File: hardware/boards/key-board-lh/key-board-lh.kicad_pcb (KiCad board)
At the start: 2 copper layers, 84 x 42 mm, 35 parts

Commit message: LH key board: every key's network identical round its switch; no acid traps; silk both sides
Owner: "the components for keys should be exactly spaced the exact same
way around every single key".
- layout.yaml networks: is ONE pattern relative to each key's switch (from
  the body CAD): the T's junction 10 mm along the body, S and P across it,
  C toward the key. On this board the one offset that clears every
  switch's pins and pole, J-CHAIN, the test pads, the register, the
  standoffs and the edge for all five keys; except: holds any key that
  cannot take it, with its reason (none here).
- Their silk letters and key name are one fixed arrangement round each T;
  a label that does not fit stops the layout rather than wandering.
- Test pads in the register's pin order (SER, QH ... 3V3), and route_first
  for the nets that reach J-CHAIN's far row, which only its back can reach.

Traces: 0 acute junctions (were 4), and a new pcb.py check fails on any -
verified to report all four on the previous board. Stitching vias keep 90
degrees from every track already on a pad (a routed pad goes without one
rather than make a wedge); a route joining the tree at a bend is squared
to a right-angle T where its clearance allows.

Silkscreen: the switch side now carries each key's name, J-CHAIN's pin-1
dot and mouth arrow (it is soldered from that side), MOUTH and the title;
the parts side adds CB DNP and MOUTH. Labels keep 0.25 mm apart and off
every pad and hole, the title lines 1.8 lines apart (0.117 mm failed).

Co-Authored-By: Claude Opus 5.5 <noreply@anthropic.com>
Claude-Session: https://claude.ai/code/session_01LmB4muFXnoLprWX4JzuJ5A
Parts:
- moved R-KEY-SER-LH5 18.6 mm to (178.0, 115.2), turned to 90 degrees
- moved R-KEY-SER-LH4 17.9 mm to (178.0, 133.2), turned to 90 degrees
- moved TP-3V3-LH 15.5 mm to (160.5, 114.0)
- moved R-KEY-PU-LH2 15.5 mm to (140.0, 118.8), turned to 90 degrees
- moved R-KEY-PU-LH3 15.5 mm to (160.0, 118.8), turned to 90 degrees
- moved C-KEY-LH2 15.5 mm to (137.3, 121.5), turned to 180 degrees
- moved C-KEY-LH3 15.5 mm to (157.3, 121.5), turned to 180 degrees
- moved R-KEY-SER-LH1 15.4 mm to (120.0, 124.2), turned to 90 degrees
- moved R-KEY-SER-LH2 15.2 mm to (140.0, 124.2), turned to 90 degrees
- moved R-KEY-SER-LH3 15.2 mm to (160.0, 124.2), turned to 90 degrees
- moved C-KEY-LH5 14.2 mm to (175.3, 112.5), turned to 180 degrees
- moved C-KEY-LH4 13.8 mm to (175.3, 130.5), turned to 180 degrees
- moved TP-QH-LH 12.5 mm to (146.5, 114.0)
- moved R-KEY-PU-LH5 11.4 mm to (178.0, 109.8), turned to 90 degrees
- moved C-KEY-LH1 11.4 mm to (117.3, 121.5), turned to 180 degrees
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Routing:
- net GND_CHAIN: track 212.8 -> 177.7 mm, vias 22 -> 11
- net /KEY_LH4: track 28.6 -> 49.6 mm
- net /KEY_LH5: track 19.3 -> 37.7 mm, vias 0 -> 2
- net V3V3_CHAIN_LH: track 137.3 -> 119.3 mm, vias 10 -> 3
- net /LH2/SWITCH_LEG: track 5.81 -> 17.4 mm, vias 0 -> 1
- net /LH3/SWITCH_LEG: track 5.81 -> 17.4 mm, vias 0 -> 1
- net /KEY_LH2: track 38.3 -> 26.9 mm, vias 0 -> 2
- net /KEY_LH3: track 32.1 -> 24.6 mm
- net /LH1/SWITCH_LEG: track 10.2 -> 17.4 mm, vias 0 -> 1
- net /CHAIN_SCK: track 36.3 -> 30.7 mm, vias 2 -> 1
- net /LH5/SWITCH_LEG: track 11.5 -> 16.8 mm, vias 0 -> 2
- net /KEY_LH1: track 49.2 -> 43.9 mm
- net /HOP_LH_LT: track 41.5 -> 36.4 mm, vias 1 -> 5
- net /CHAIN_SER_LH: track 35.1 -> 38.5 mm, vias 0 -> 2
- net /LH4/SWITCH_LEG: track 11.8 -> 14.9 mm, vias 0 -> 1
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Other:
- board text added: "CB DNP"
- board text added: "MOUTH"

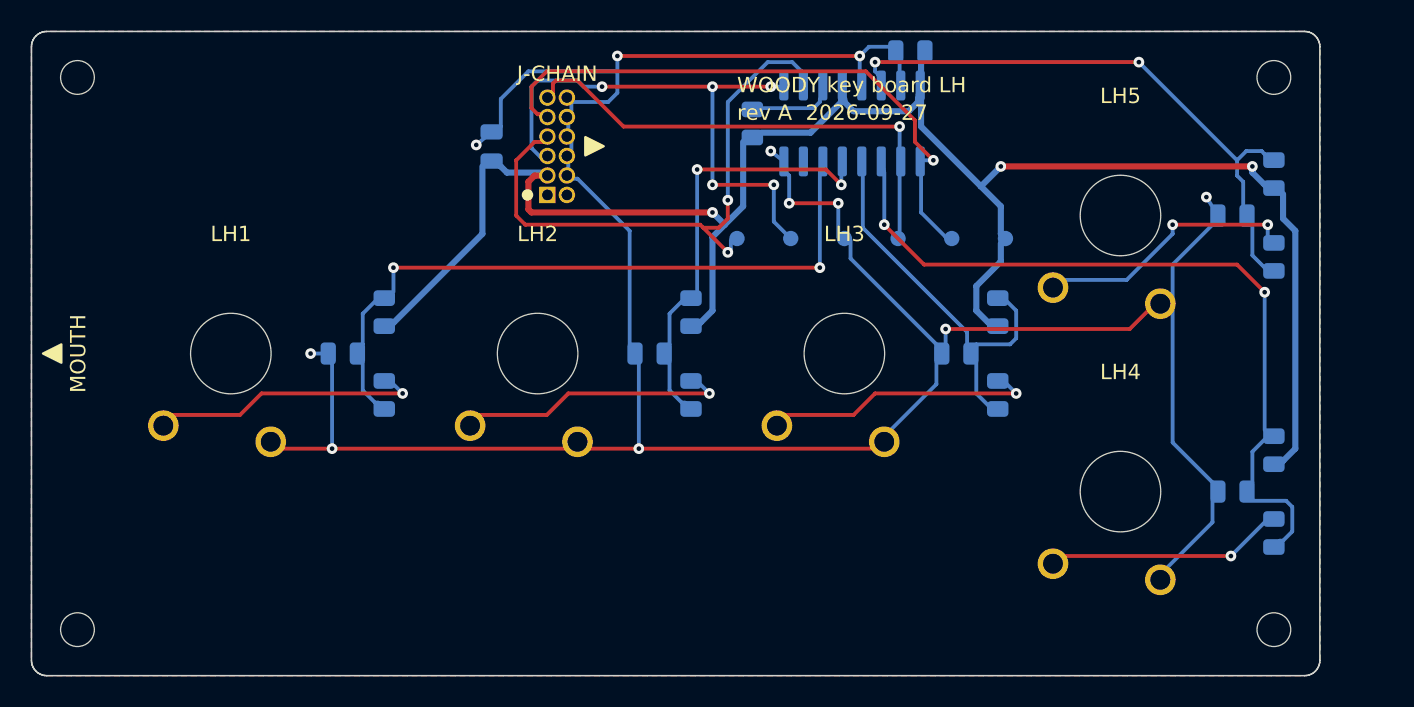
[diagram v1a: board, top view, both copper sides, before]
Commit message: Wave r2 fixes, part 1: board tools, the T's orientation, the decoupling loop; docs
Tools (docs/review/2026-09-27-lh-key-board-r2, closed by id in its STATUS.md):
- network_parts: the axis-y rotation was the wrong way round (R6-3), so
  every S and P faced its KEY pad away from the junction; fixed, with a
  layout-time assert that each T's three nearest pads are its node, and
  validation of networks: (R6-9).
- check_tracks sees a branch ending mid-track, and exempts a wedge whose
  apex a via or pad fills (R6-1, R6-7, R3-4); square_joins splits such a
  track first, keeps the router's copper list current, tests holes,
  keep-outs and the edge, and warns at its pass limit (R6-6).
- Vias keep off silkscreen (the router takes the silk as via obstacles),
  and check_silk fails silk on a via and filled slivers (R3-2, R3-3, R6-8,
  R6-13).
- Any DRC test set to ignore fails unless allowlisted with its reason
  (R6-2); check proves the standoff keep-outs hold no copper and the holes
  are NPTH at the CAD's size (R6-4).
- connect_first: the decoupler's return routed first to the register's
  ground pin 8 (not pin 15, CLK INH), held to 15 mm by check (R3-1) - now
  10.4 mm of track.
- Stitching vias skipped only on the main ground tree (R6-5); one stub per
  pad (R3-7); silk stroke 0.18 (R3-8); removed library silk is reported
  (R6-12). Test pads QH/SER in pin order (R3-9).

Docs (R1, R5 non-mechanical): the glitch-filter, lumped-load, R-KEY-SER
ceiling and scan-latency arguments restated against the right limits;
forbidden patterns for the retired thresholds in their CSV spellings.

Co-Authored-By: Claude Opus 5.5 <noreply@anthropic.com>
Claude-Session: https://claude.ai/code/session_01LmB4muFXnoLprWX4JzuJ5A
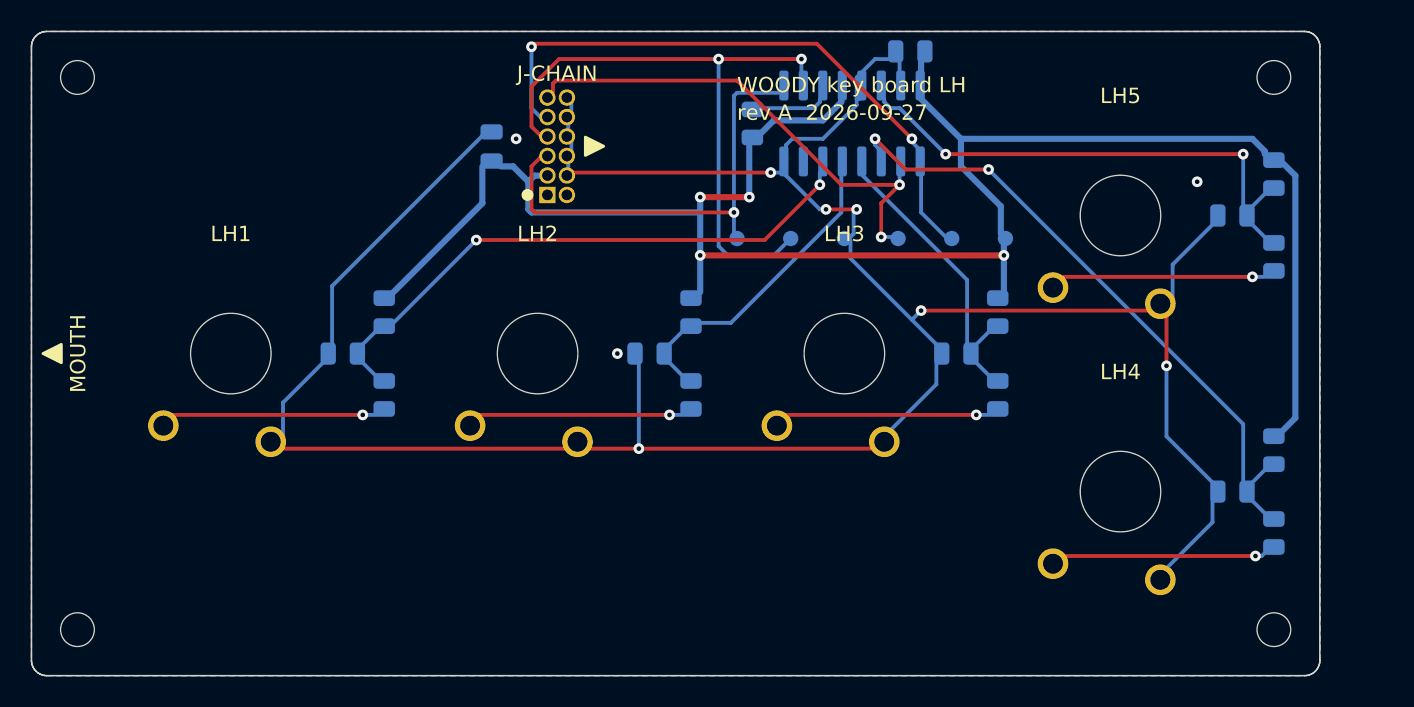
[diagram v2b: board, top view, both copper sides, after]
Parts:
- moved TP-QH-LH 3.50 mm to (143.0, 114.0)
- moved TP-SER-LH 3.50 mm to (146.5, 114.0)
- turned R-KEY-PU-LH1 to -90 degrees
- turned R-KEY-PU-LH2 to -90 degrees
- turned R-KEY-PU-LH3 to -90 degrees
- turned R-KEY-PU-LH4 to -90 degrees
- turned R-KEY-PU-LH5 to -90 degrees
- turned R-KEY-SER-LH1 to -90 degrees
- turned R-KEY-SER-LH2 to -90 degrees
- turned R-KEY-SER-LH3 to -90 degrees
- turned R-KEY-SER-LH4 to -90 degrees
- turned R-KEY-SER-LH5 to -90 degrees
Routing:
- net GND_CHAIN: track 177.7 -> 155.2 mm, vias 11 -> 9
- net /KEY_LH4: track 49.6 -> 38.4 mm
- net /KEY_LH2: track 26.9 -> 17.0 mm, vias 2 -> 0
- net /KEY_LH1: track 43.9 -> 34.6 mm
- net /KEY_LH3: track 24.6 -> 16.3 mm
- net /HOP_LH_LT: track 36.4 -> 29.2 mm, vias 5 -> 1
- net /KEY_LH5: track 37.7 -> 30.7 mm
- net /LH1/SWITCH_LEG: track 17.4 -> 13.2 mm
- net /LH2/SWITCH_LEG: track 17.4 -> 13.2 mm
- net /LH3/SWITCH_LEG: track 17.4 -> 13.2 mm
- net /LH5/SWITCH_LEG: track 16.8 -> 13.2 mm, vias 2 -> 1
- net /LH4/SWITCH_LEG: track 14.9 -> 13.1 mm
- net /CHAIN_SER_LH: track 38.5 -> 40.0 mm
- net /CHAIN_SCK: track 30.7 -> 31.6 mm, vias 1 -> 2
- net /CHAIN_SHLD: track 38.6 -> 37.9 mm, vias 1 -> 2
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
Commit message: Key boards hang on screws through the wood: the owner's standard
The corner mount is now an M2x8 ISO 4762 screw down a 1/4 in plugged bore in
the wood top, its head on the plate; a Wurth 2.0 mm spacer and an ISO 7092
washer below the plate set the board's depth (3.5 below the seat); an
ISO 4032 nut on the board's underside. Replaces the PEM MSO4 standoff.

- body.yaml: new hardware.kb_* mount parameters, each sourced to a banked
  drawing; kb_tail_margin (the tail corners' bores must clear the last cap
  slot); kb_mount_inset 3.4 (the bores must clear the side grooves).
- Model: bores in the oak top, plate clearance holes, plug/screw/spacer/
  washer/nut solids; DRC rules for depth and its tolerance stack, head on
  plate metal, spacer clear of cutouts, wood round each bore, plug depth,
  thread past the nut, screw end clear of the main board, nuts clear of
  the chain header. New figure: section-kb-mount.
- PCB keep-outs from the nut (bottom) and spacer/washer (top), grown by
  the mount float. LH board re-laid out: check 0 errors.
- Banked 13 datasheets (fragment R14): spacer, screw, nut, washer, plug
  cutter, Samsung 10 uF spec sheet, Gateron -Y31 spec.

Co-Authored-By: Claude Opus 5.5 <noreply@anthropic.com>
Claude-Session: https://claude.ai/code/session_01LmB4muFXnoLprWX4JzuJ5A
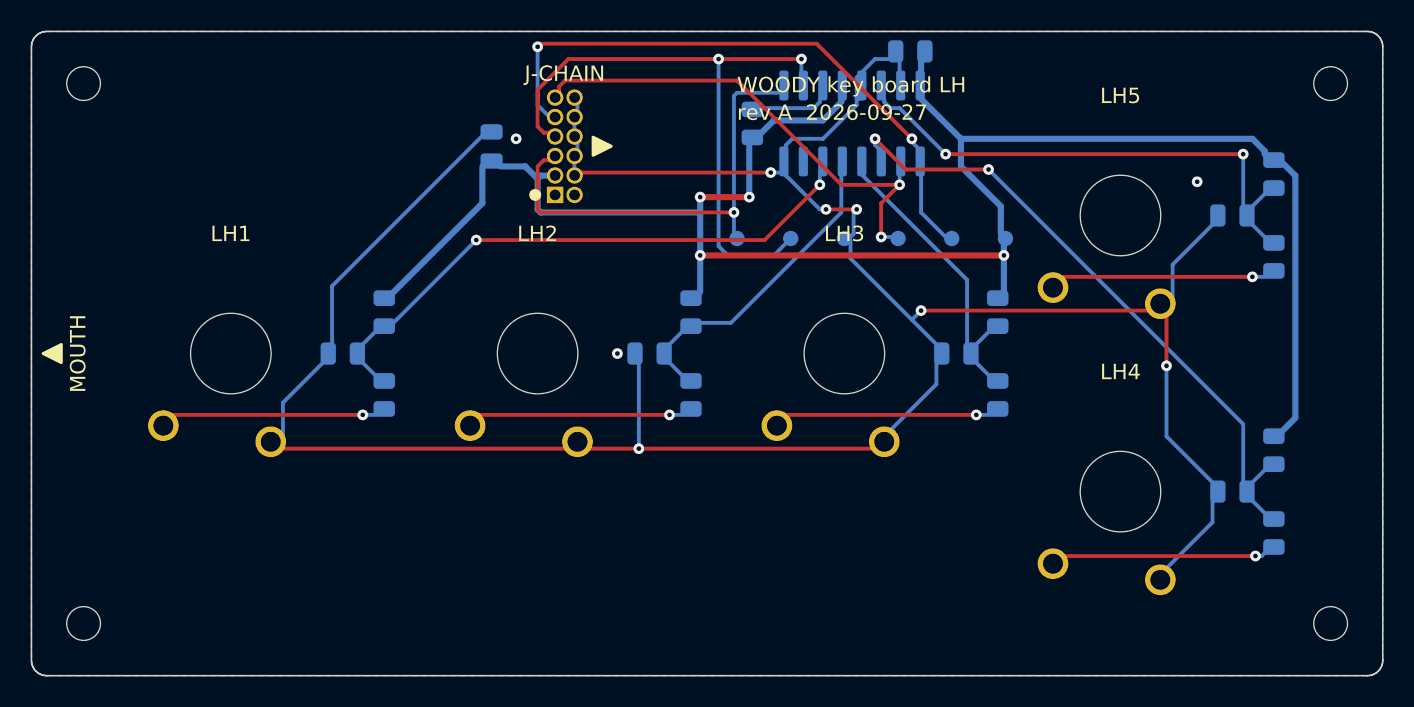
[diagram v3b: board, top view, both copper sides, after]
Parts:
- H1, H2, H3, H4: value M2 standoff -> M2 mount
- moved H3 3.72 mm to (181.7, 139.1)
- moved H4 3.72 mm to (181.7, 103.9)
- moved H1 0.57 mm to (100.4, 139.1)
- moved H2 0.57 mm to (100.4, 103.9)
- moved J-CHAIN 0.50 mm to (131.1, 111.2)
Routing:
- net GND_CHAIN: track 155.2 -> 154.4 mm
- net /CHAIN_SCK: track 31.6 -> 31.1 mm
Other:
- board size 84 x 42 mm -> 88.1 x 42 mm

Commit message: Key boards: numeric references on every part, silkscreen readable with parts fitted
Owner, 2026-09-28: 'resistors should all be R1, R2, R3 etc. Everything should
be properly numeric and labeled on the silk screen', and 'make sure silk
screens will still be visible even when components are placed'.

- Sheets: the key boards' instance references renumbered (SWn, R(2n-1)
  series, R(2n) pull-up, Cn per key; then the free pull-up, decoupler,
  bulk cap, U1, J1, TP1-TP6). Circuit-level row names are unchanged; each
  part's BOM row stays its Row field. Test pads carry a Probe field.
- Tools find parts by row and sheet, not by name: pcb.py ref_of (placement,
  the network T, check_cad), kicad.py's allocation and chain checks. The
  allocation check now fails a board with no register instead of passing it
  by finding none. The board export records each part's sheet.
- Silkscreen: every part's reference, sized by its real width in KiCad's
  font (text_w; the old per-character guess ran 15-35 % short); network
  resistors' references read along the parts; switches 'SW1 LH1'; a
  test-pad legend (TP1 QH ...). check_silk now fails any placed mark under a
  part's courtyard, proven on a scratch copy on both sides.
- KS-33 footprint courtyard +-7.0 -> +-7.75: the switch is 15 x 15, and the
  old courtyard let labels sit under its housing.
- Straight-down plan renders of both sides (pcb-plan-top/-bottom.png).
- LH board re-laid out: check 0 errors; README and tooling.md follow.

Co-Authored-By: Claude Opus 5.5 <noreply@anthropic.com>
Claude-Session: https://claude.ai/code/session_01LmB4muFXnoLprWX4JzuJ5A
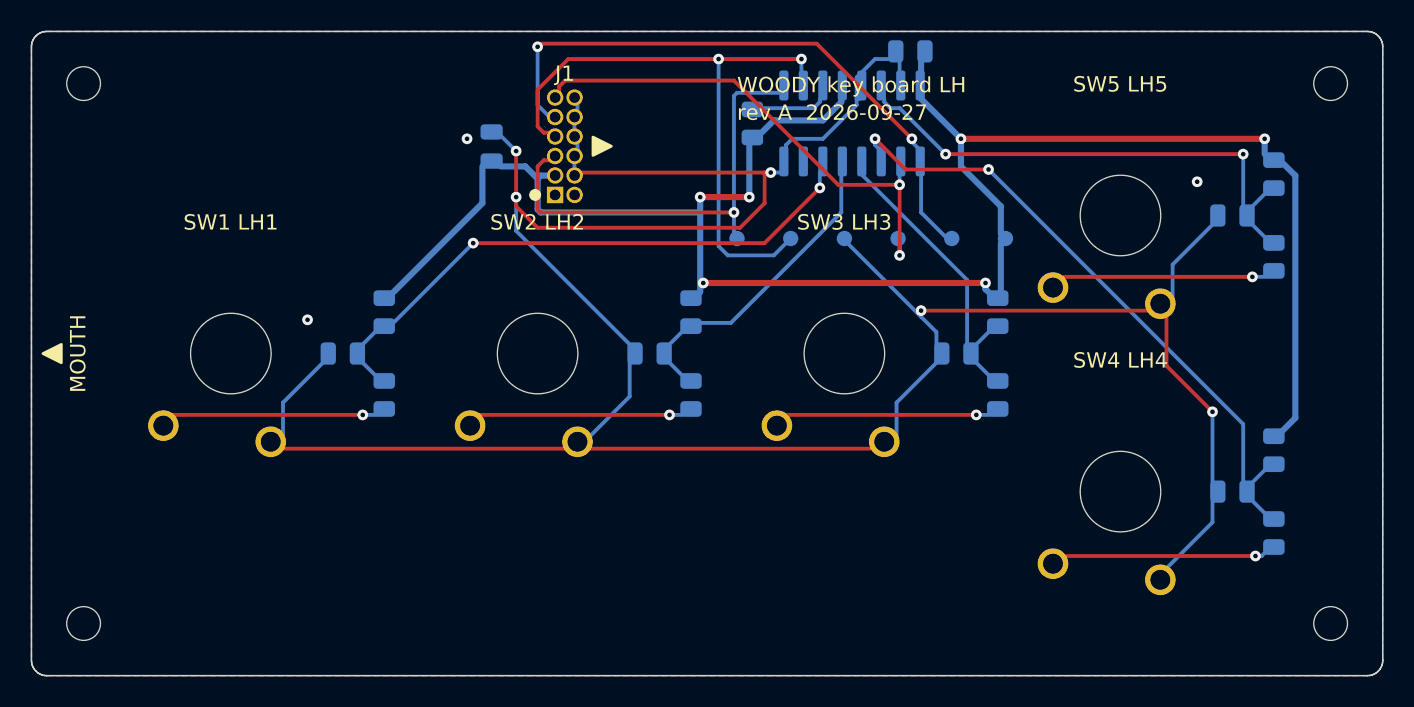
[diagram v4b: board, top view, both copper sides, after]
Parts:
- removed C-BULK-CHAIN-LH: 10uF DNP, Capacitor_SMD:C_0805_2012Metric
- removed C-DECOUPLE-165-LH: 100nF, Capacitor_SMD:C_0805_2012Metric
- removed C-KEY-LH1, C-KEY-LH2, C-KEY-LH3, C-KEY-LH4, C-KEY-LH5: 47nF, Capacitor_SMD:C_0805_2012Metric
- removed J-CHAIN: 12-way, woody:IDC-Header_2x06_P1.27mm_Samtec_SHF_Horizontal
- removed R-KEY-PU-FREE3, R-KEY-PU-LH1, R-KEY-PU-LH2, R-KEY-PU-LH3, R-KEY-PU-LH4, R-KEY-PU-LH5: 2k2 1%, Resistor_SMD:R_0805_2012Metric
- removed R-KEY-SER-LH1, R-KEY-SER-LH2, R-KEY-SER-LH3, R-KEY-SER-LH4, R-KEY-SER-LH5: 100R 1%, Resistor_SMD:R_0805_2012Metric
- removed SW-LH1, SW-LH2, SW-LH3, SW-LH4, SW-LH5: KS-33, woody:SW_Gateron_KS33_1u
- removed TP-3V3-LH, TP-GND-LH, TP-QH-LH, TP-SCK-LH, TP-SER-LH, TP-SHLD-LH: test pad, TestPoint:TestPoint_Pad_D1.0mm
- removed U-KEYS-LH: 74HCS165, Package_SO:SOIC-16_3.9x9.9mm_P1.27mm
- added C1: 47nF, Capacitor_SMD:C_0805_2012Metric, B.Cu at (117.3, 121.5)
- added C2: 47nF, Capacitor_SMD:C_0805_2012Metric, B.Cu at (137.3, 121.5)
- added C3: 47nF, Capacitor_SMD:C_0805_2012Metric, B.Cu at (157.3, 121.5)
- added C4: 47nF, Capacitor_SMD:C_0805_2012Metric, B.Cu at (175.3, 130.5)
- added C5: 47nF, Capacitor_SMD:C_0805_2012Metric, B.Cu at (175.3, 112.5)
- added C6: 100nF, Capacitor_SMD:C_0805_2012Metric, B.Cu at (154.3, 101.8)
- added C7: 10uF DNP, Capacitor_SMD:C_0805_2012Metric, B.Cu at (127.0, 108.0)
- added J1: 12-way, woody:IDC-Header_2x06_P1.27mm_Samtec_SHF_Horizontal, B.Cu at (131.1, 111.2)
- added R1: 100R 1%, Resistor_SMD:R_0805_2012Metric, B.Cu at (120.0, 124.2)
- added R10: 2k2 1%, Resistor_SMD:R_0805_2012Metric, B.Cu at (178.0, 109.8)
- added R11: 2k2 1%, Resistor_SMD:R_0805_2012Metric, B.Cu at (144.0, 106.5)
- added R2: 2k2 1%, Resistor_SMD:R_0805_2012Metric, B.Cu at (120.0, 118.8)
- added R3: 100R 1%, Resistor_SMD:R_0805_2012Metric, B.Cu at (140.0, 124.2)
- added R4: 2k2 1%, Resistor_SMD:R_0805_2012Metric, B.Cu at (140.0, 118.8)
- added R5: 100R 1%, Resistor_SMD:R_0805_2012Metric, B.Cu at (160.0, 124.2)
- added R6: 2k2 1%, Resistor_SMD:R_0805_2012Metric, B.Cu at (160.0, 118.8)
- added R7: 100R 1%, Resistor_SMD:R_0805_2012Metric, B.Cu at (178.0, 133.2)
- added R8: 2k2 1%, Resistor_SMD:R_0805_2012Metric, B.Cu at (178.0, 127.8)
- added R9: 100R 1%, Resistor_SMD:R_0805_2012Metric, B.Cu at (178.0, 115.2)
- added SW1: KS-33, woody:SW_Gateron_KS33_1u, F.Cu at (110.0, 121.5)
- added SW2: KS-33, woody:SW_Gateron_KS33_1u, F.Cu at (130.0, 121.5)
- added SW3: KS-33, woody:SW_Gateron_KS33_1u, F.Cu at (150.0, 121.5)
- added SW4: KS-33, woody:SW_Gateron_KS33_1u, F.Cu at (168.0, 130.5)
- added SW5: KS-33, woody:SW_Gateron_KS33_1u, F.Cu at (168.0, 112.5)
- added TP1: test pad, TestPoint:TestPoint_Pad_D1.0mm, B.Cu at (143.0, 114.0)
- added TP2: test pad, TestPoint:TestPoint_Pad_D1.0mm, B.Cu at (146.5, 114.0)
- added TP3: test pad, TestPoint:TestPoint_Pad_D1.0mm, B.Cu at (150.0, 114.0)
- added TP4: test pad, TestPoint:TestPoint_Pad_D1.0mm, B.Cu at (153.5, 114.0)
- added TP5: test pad, TestPoint:TestPoint_Pad_D1.0mm, B.Cu at (157.0, 114.0)
- added TP6: test pad, TestPoint:TestPoint_Pad_D1.0mm, B.Cu at (160.5, 114.0)
- added U1: 74HCS165, Package_SO:SOIC-16_3.9x9.9mm_P1.27mm, B.Cu at (150.5, 106.5)
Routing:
- net GND_CHAIN: track 154.4 -> 166.1 mm, vias 9 -> 8
- net /CHAIN_SCK: track 31.1 -> 31.8 mm
- net V3V3_CHAIN_LH: track 119.5 -> 119.4 mm, vias 4 -> 6
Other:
- board text added: "C1"
- board text added: "C2"
- board text added: "C3"
- board text added: "C4"
- board text added: "C5"
- board text added: "C6"
- board text added: "C7 DNP"
- board text added: "J1"
- board text added: "R1"
- board text added: "R10"
- board text added: "R11"
- board text added: "R2"
- board text added: "R3"
- board text added: "R4"
- board text added: "R5"
- board text added: "R6"
- board text added: "R7"
- board text added: "R8"
- board text added: "R9"
- board text added: "SW1 LH1"
- board text added: "SW2 LH2"
- board text added: "SW3 LH3"
- board text added: "SW4 LH4"
- board text added: "SW5 LH5"
- board text added: "TP1"
- board text added: "TP1 QH TP2 SER TP3 GND"
- board text added: "TP2"
- board text added: "TP3"
- board text added: "TP4"
- board text added: "TP4 SCK TP5 SH/LD TP6 3V3"
- board text added: "TP5"
- board text added: "TP6"
- board text added: "U1"
- board text removed: "3V3"
- board text removed: "74HCS165"
- board text removed: "C"
- board text removed: "CB DNP"
- board text removed: "CD"
- board text removed: "GND"
- board text removed: "J-CHAIN"
- board text removed: "P"
- board text removed: "PF"
- board text removed: "QH"
- board text removed: "S"
- board text removed: "SCK"
- board text removed: "SER"
- board text removed: "SH/LD"
